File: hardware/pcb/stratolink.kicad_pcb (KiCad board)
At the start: 2 copper layers, 23.4 x 57.3 mm, 62 parts, among them J1 Conn_Header_JST_PH_1x02_P2mm_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, J2 Conn_Header_JST_PH_1x02_P2mm_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, J20 Conn_ARM_SWD_TagConnect_TC203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, J3 Conn_PinHeader_1x07_P2.54mm_V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, J4 Conn_PinHeader_1x07_P2.54mm_V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, U2 RAK3172, U5 TMP117NAIYBGR, U7 LIS2DH12TR

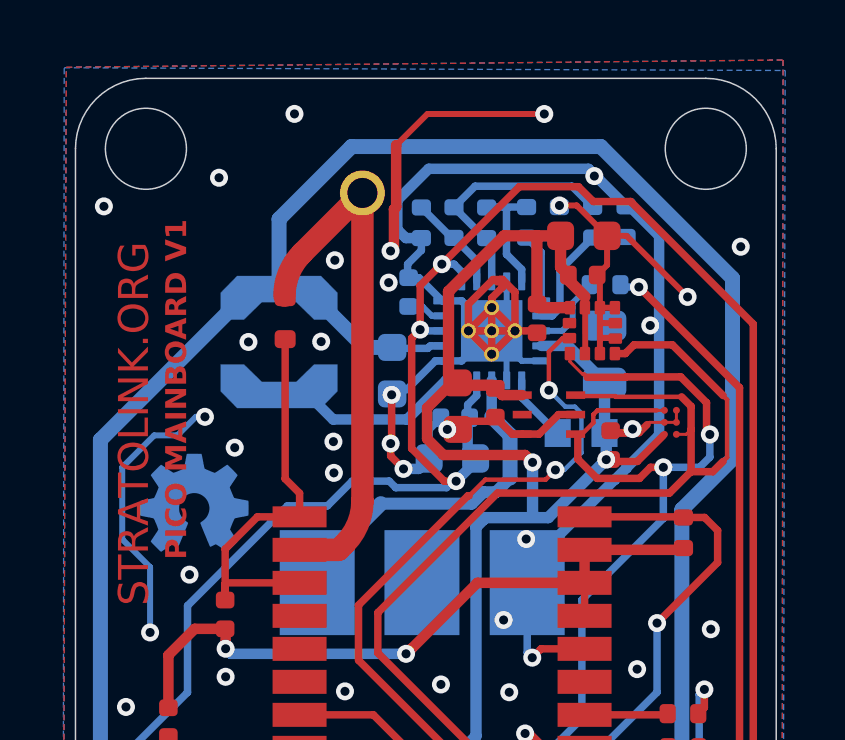
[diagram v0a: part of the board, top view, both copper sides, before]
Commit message: hardware: start v1.1 with corrected TMP117 symbol and routing
Use hardware/pcb as the canonical working project. Preserve component placement, correct the DSBGA ball map and local copper, add the v1.1/v2 checklist and canonical-path verification records. PCB saved in KiCad 10 format.
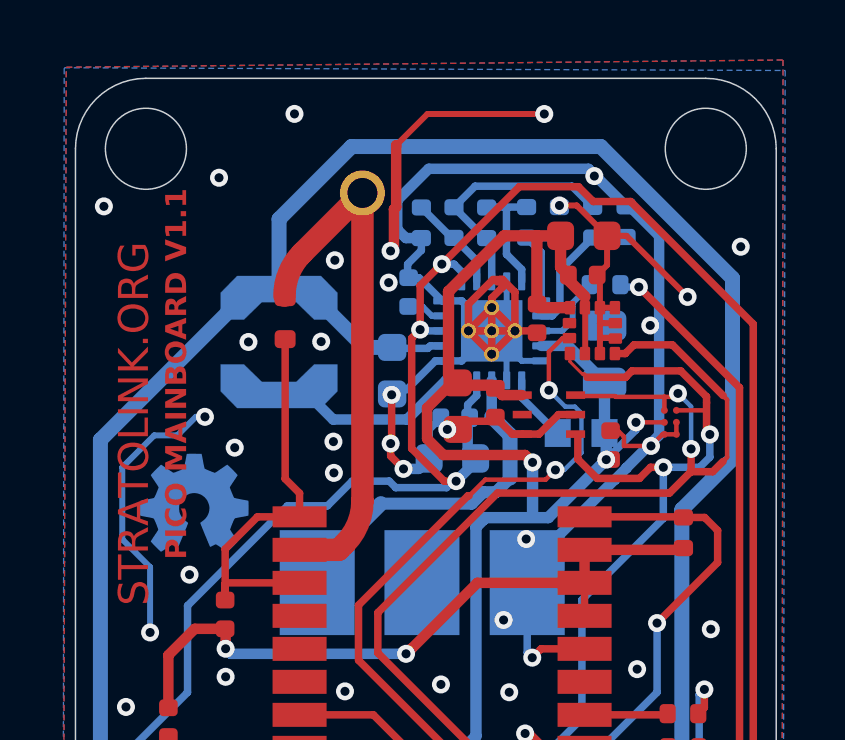
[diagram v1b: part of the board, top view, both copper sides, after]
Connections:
- U5 pad A1: SCL -> SDA
- U5 pad A2: GND -> SCL
- U5 pad B1: GND -> +3.3V
- U5 pad C1: +3.3V -> GND
- U5 pad C2: SDA -> GND
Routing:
- net SCL: track 98.6 -> 96.5 mm
- net +3.3V: track 141.8 -> 142.2 mm, vias 6 -> 7
- net SDA: vias 2 -> 4
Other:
- board text added: "PICO MAINBOARD V1.1"
- board text removed: "PICO MAINBOARD V1"

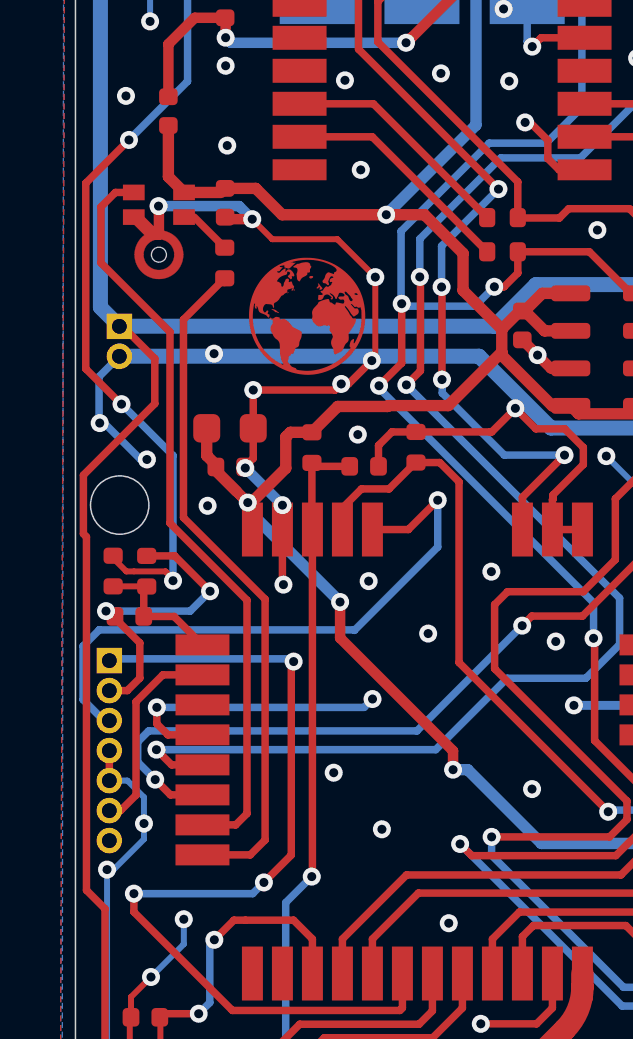
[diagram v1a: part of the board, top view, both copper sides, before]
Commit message: hardware: remove microphone from v1.1 payload
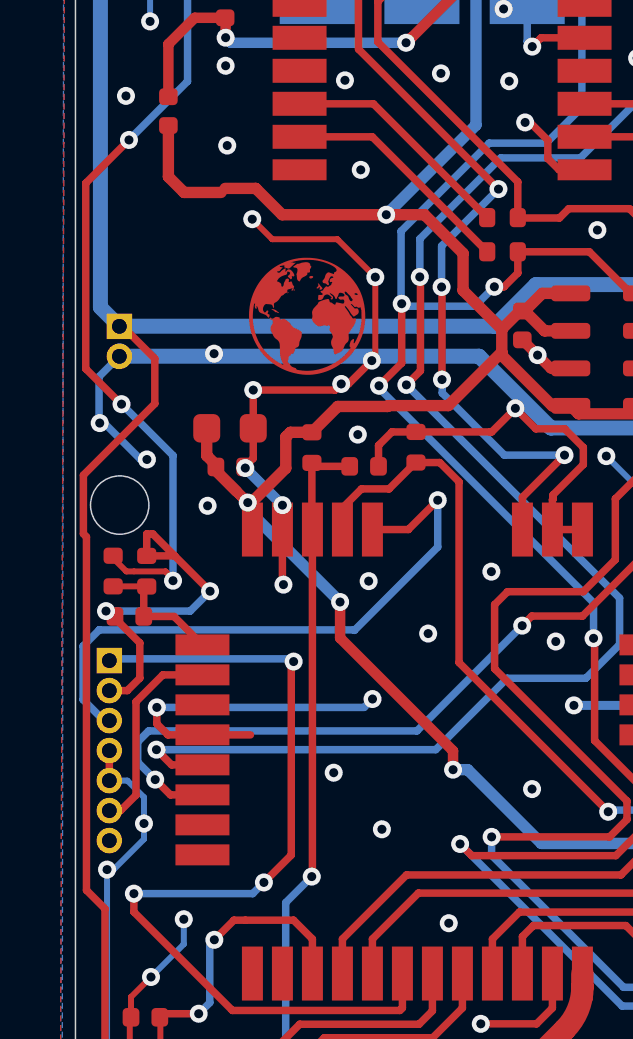
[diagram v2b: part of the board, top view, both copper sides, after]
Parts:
- removed C13: 100nF, Capacitor_SMD:C_0402_1005Metric
- removed MK1: T3902, lib:MIC_T3902
- removed R20: 33Ω, Resistor_SMD:R_0402_1005Metric
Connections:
- U2 pad 31: PDM -> unconnected-(U2-PB4/ADC2-Pad31)
- U2 pad 32: CLK -> unconnected-(U2-PB3/ADC1-Pad32)
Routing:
- net PDM: track 25.2 -> 0.00 mm
- net CLK: track 22.9 -> 0.00 mm
- net GND: track 265.5 -> 261.7 mm, vias 85 -> 84
- net Net-(MK1-CLK): track 1.44 -> 0.00 mm

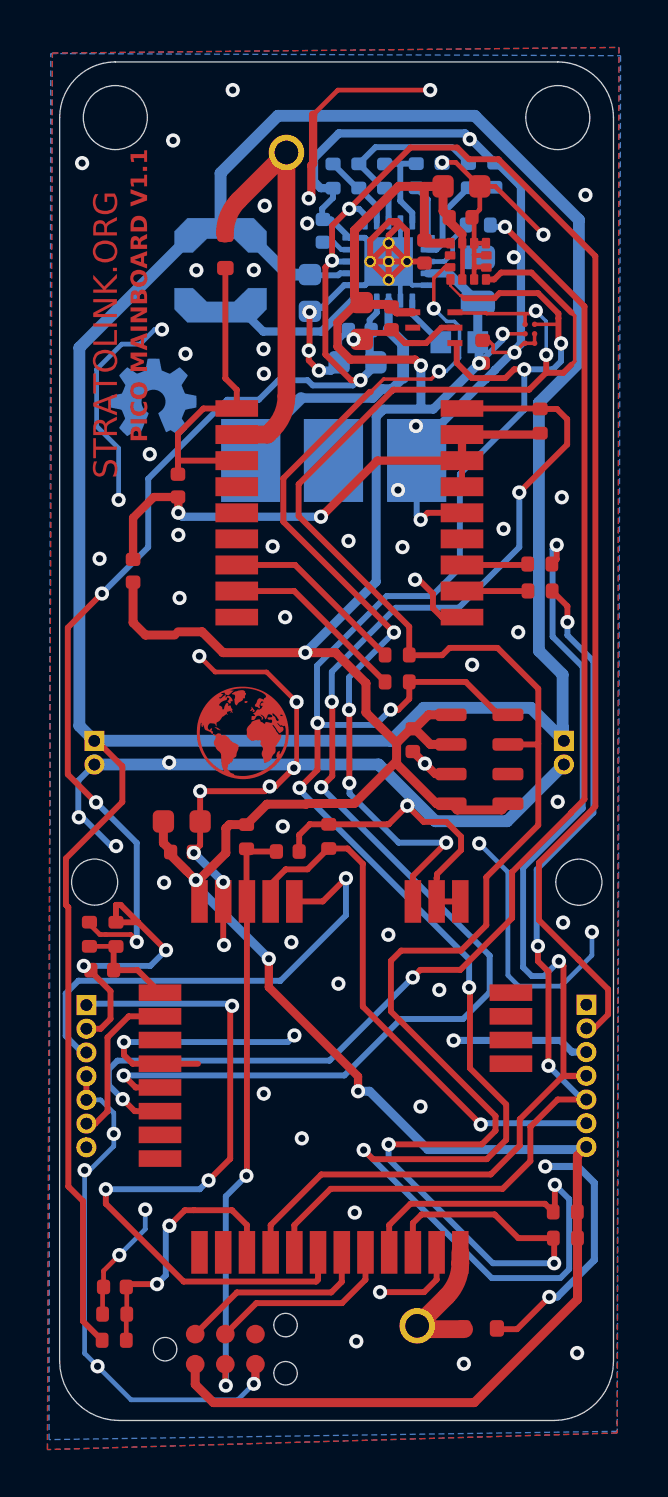
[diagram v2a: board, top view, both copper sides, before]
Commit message: hardware: add v1.1 side solar solder mounts
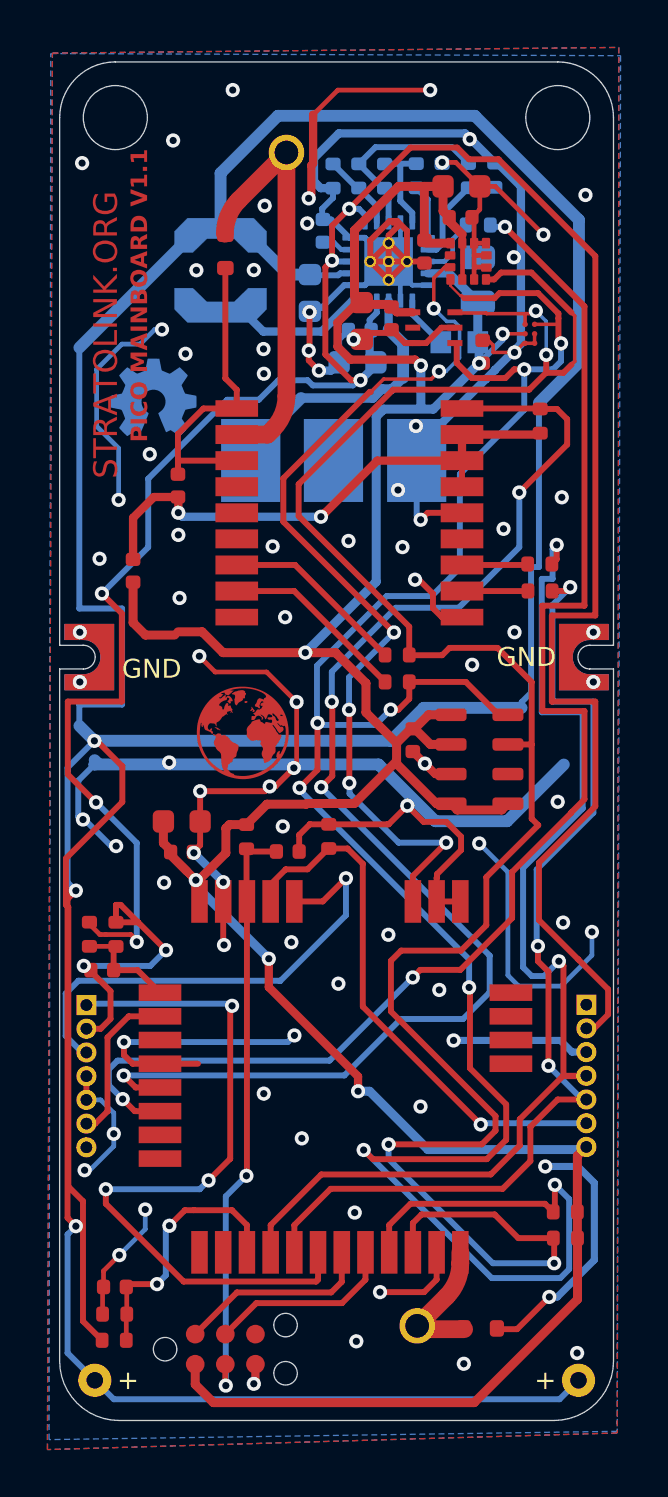
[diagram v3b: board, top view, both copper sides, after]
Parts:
- J1: value Conn_Header_JST_PH_1x02_P2mm_Vertical_SMD -> Solar panel direct solder; footprint Connector_PinHeader_1.00mm:PinHeader_1x02_P1.00mm_Vertical -> lib:Solar_Notch_Right_1p0x1p5; moved to F.Cu
- J2: value Conn_Header_JST_PH_1x02_P2mm_Vertical_SMD -> Solar panel direct solder; footprint Connector_PinHeader_1.00mm:PinHeader_1x02_P1.00mm_Vertical -> lib:Solar_Notch_Left_1p0x1p5; moved to F.Cu
- moved J1 4.10 mm to (76.7, 54.5), turned to 0 degrees
- moved J2 3.82 mm to (53.3, 54.5), turned to 0 degrees
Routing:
- net +SOLAR: track 123.8 -> 172.6 mm, vias 0 -> 3
- net GND: track 261.7 -> 246.0 mm, vias 84 -> 87
- net VSTOR: track 98.3 -> 104.0 mm
- net PB5: track 55.4 -> 59.0 mm
- net RX: track 40.5 -> 42.8 mm
- net TX: track 45.8 -> 47.5 mm
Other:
- outline, holes or cut-outs redrawn
- board text added: "+"
- board text added: "GND"
